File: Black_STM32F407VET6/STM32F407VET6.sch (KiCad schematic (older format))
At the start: 93 parts, among them J1 T0, J10 - HotBed +, J11 Heater0, J12 X-, J13 Y-, J14 Z-, J15 Z+, J16 USB_B, J2 T1, J22 Left, J23 EXP2, J24 LCD2004, J25 Bottom, J26 Right, J28 LIGHTS, J29 Z, J3 TB, J30 Z, J38 X, J39 Y, J4 TC, J41 E0, J43 Heater1, J44 COM, J47 I2C, J48 SPI, J49 SPI, J5 + VIN -, J50 SDIO, J51 Servo, J52 Servo, J53 PowerSelect, J54 Power, J55 PD11, J56 Power, J6 Fan3, J7 Fan2, J8 Fan1, J9 Fan0, Q1 BCX70, Q10 BCX70, Q11 BCX70, Q12 IRLR8726PBF, Q13 IRLR8726PBF, Q14 IRLR8726PBF, Q2 BCX70, Q3 BCX70, Q4 IRLML0030TRPBF, Q5 BCX70, Q6 IRLML0030TRPBF, Q7 IRLML0030TRPBF, Q8 IRLML0030TRPBF, Q9 BCX70, SW1 Boot0, U5 AT24CS01-SSHM

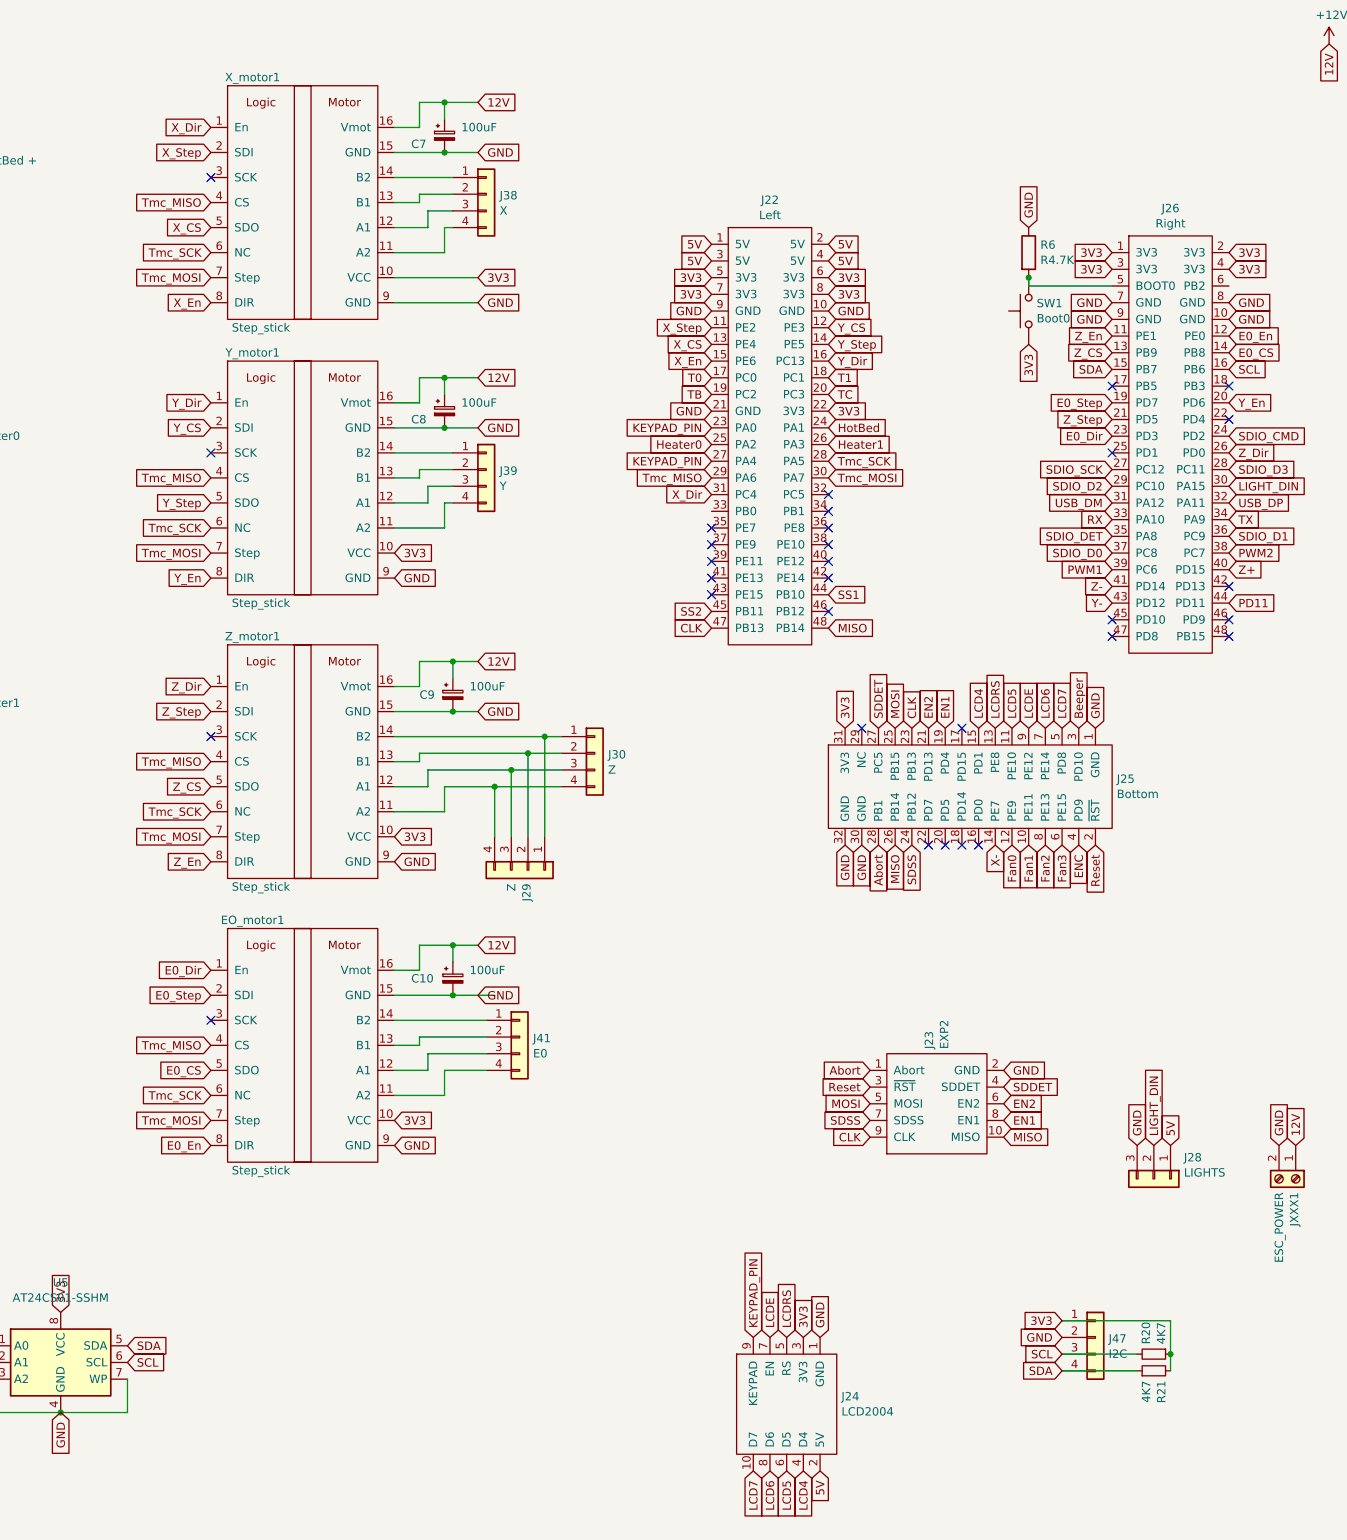
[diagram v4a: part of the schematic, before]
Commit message: Power connectors - Removed left side holes to make room for Heater and Bed traces - Moved spi connectors, temperature connectors, fan connectors - Assigned correct footprints to power connectors (KF7.62_2P) 	- Downloaded from: https://github.com/StefanHamminga/SH_Connectors.pretty
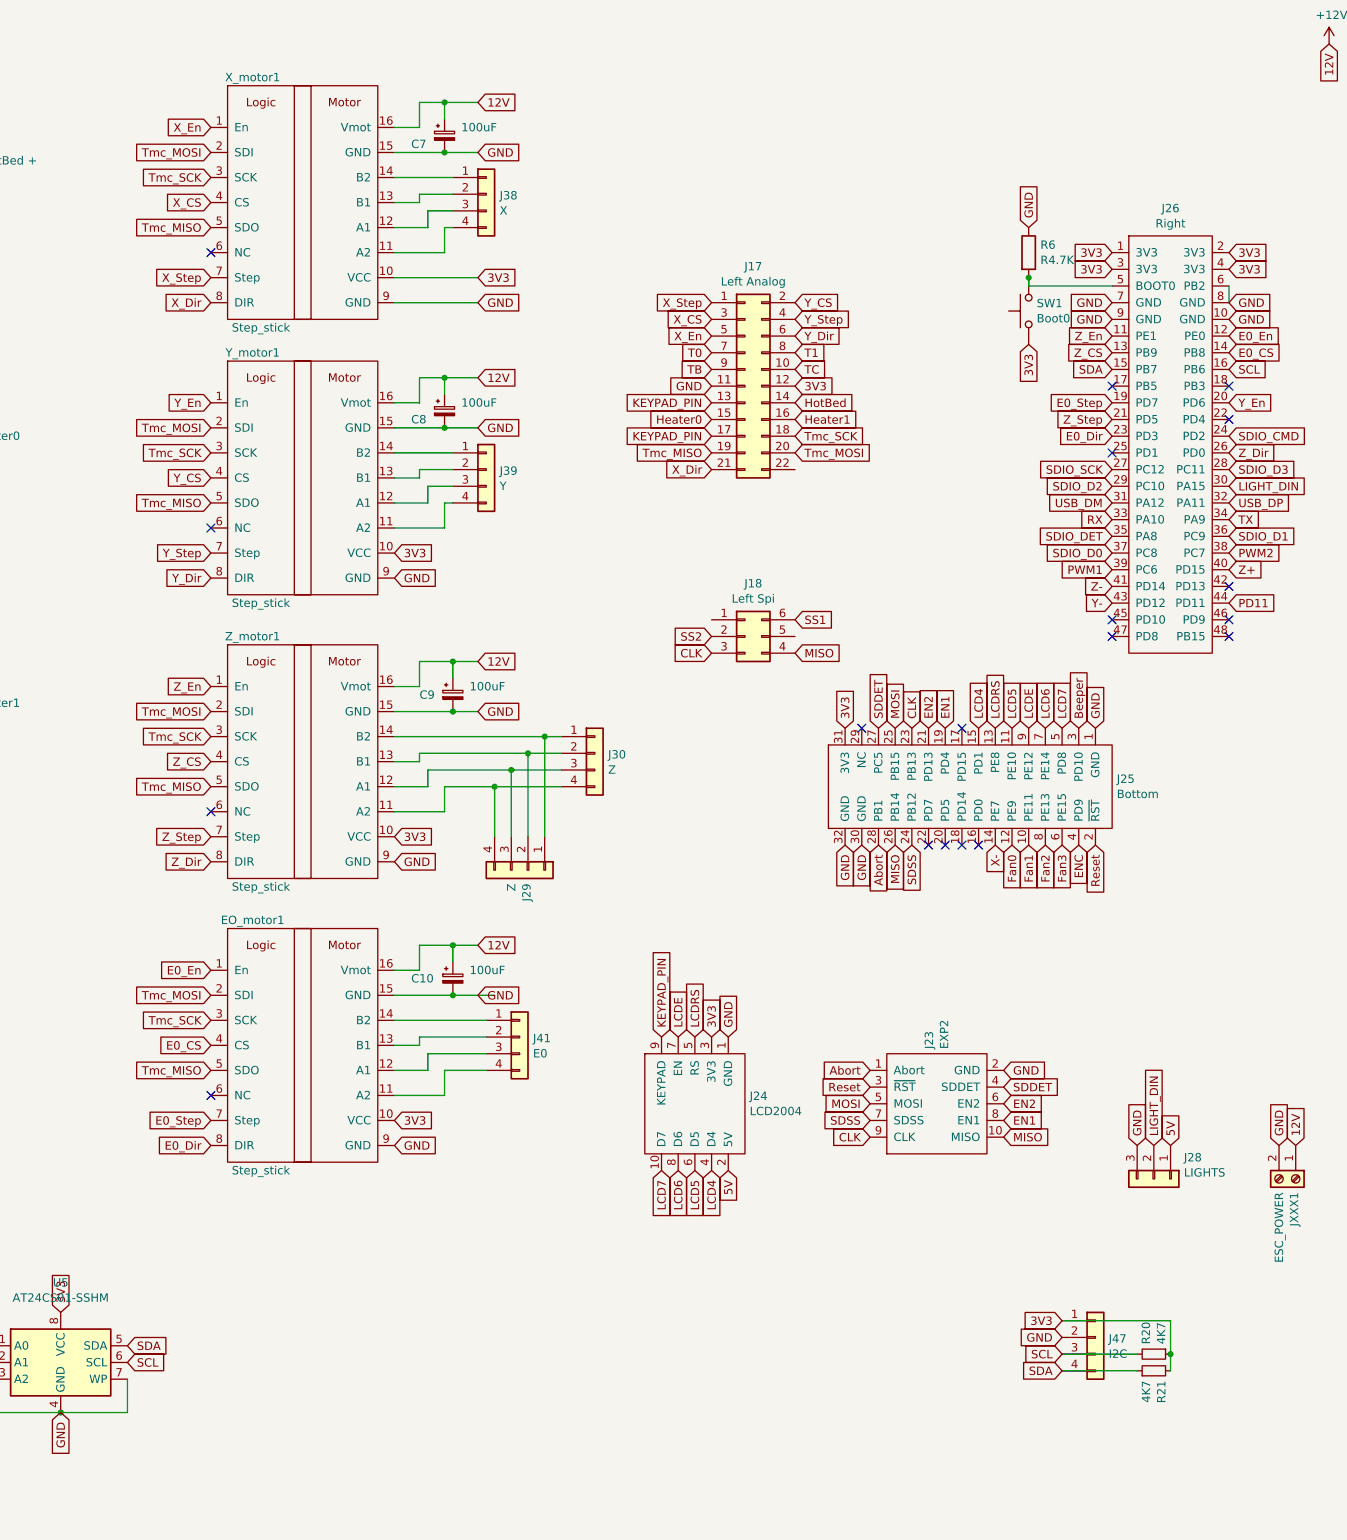
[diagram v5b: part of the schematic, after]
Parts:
- removed J22: Left, Connector_PinSocket_2.54mm:PinSocket_2x24_P2.54mm_Vertical, symbol STM32F407VET6:Left
- added J17: Left Analog, Connector_PinHeader_2.54mm:PinHeader_2x11_P2.54mm_Vertical, symbol Connector_Generic:Conn_02x11_Odd_Even
- added J18: Left Spi, Connector_PinHeader_2.54mm:PinHeader_2x03_P2.54mm_Vertical, symbol Connector_Generic:Conn_02x03_Counter_Clockwise
- J10: footprint Connector_JST:JST_XH_B2B-XH-A_1x02_P2.50mm_Vertical -> SH_Connectors:KF7.62_2P
- J11: footprint Connector_JST:JST_XH_B2B-XH-A_1x02_P2.50mm_Vertical -> TerminalBlock:TerminalBlock_bornier-2_P5.08mm
- J24: footprint Connector_JST:JST_XH_B10B-XH-A_1x10_P2.50mm_Vertical -> Connector_IDC:IDC-Header_2x05_P2.54mm_Vertical
- J43: footprint Connector_JST:JST_XH_B2B-XH-AM_1x02_P2.50mm_Vertical -> TerminalBlock:TerminalBlock_bornier-2_P5.08mm
- J5: footprint TerminalBlock_MetzConnect:TerminalBlock_MetzConnect_Type055_RT01502HDWU_1x02_P5.00mm_Horizontal -> SH_Connectors:KF7.62_2P
- JXXX1: footprint TerminalBlock_MetzConnect:TerminalBlock_MetzConnect_Type055_RT01502HDWU_1x02_P5.00mm_Horizontal -> TerminalBlock:TerminalBlock_bornier-2_P5.08mm
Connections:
- net +3V3: now also J17.12 (Pin_12)
- net CLK: now also J18.3 (Pin_3)
- net E0_CS: now also EO_motor1.4 (CS); no longer EO_motor1.5 (SDO)
- net E0_Dir: now also EO_motor1.8 (DIR); no longer EO_motor1.1 (En)
- net E0_En: now also EO_motor1.1 (En); no longer EO_motor1.8 (DIR)
- net E0_Step: now also EO_motor1.7 (Step); no longer EO_motor1.2 (SDI)
- net GND: now also J26.6 (PB2), J17.11 (Pin_11)
- net Heater0: now also J17.15 (Pin_15)
- net Heater1: now also J17.16 (Pin_16)
- net HotBed: now also J17.14 (Pin_14)
- net KEYPAD_PIN: now also J17.13 (Pin_13), J17.17 (Pin_17)
- net MISO: now also J18.4 (Pin_4)
- net SS1: now also J18.6 (Pin_6)
- net SS2: now also J18.2 (Pin_2)
- net T0: now also J17.7 (Pin_7)
- net T1: now also J17.8 (Pin_8)
- net TB: now also J17.9 (Pin_9)
- net TC: now also J17.10 (Pin_10)
- net Tmc_MISO: now also EO_motor1.5 (SDO), X_motor1.5 (SDO), Y_motor1.5 (SDO), Z_motor1.5 (SDO), J17.19 (Pin_19); no longer EO_motor1.4 (CS), X_motor1.4 (CS), Y_motor1.4 (CS), Z_motor1.4 (CS)
- net Tmc_MOSI: now also EO_motor1.2 (SDI), X_motor1.2 (SDI), Y_motor1.2 (SDI), Z_motor1.2 (SDI), J17.20 (Pin_20); no longer EO_motor1.7 (Step), X_motor1.7 (Step), Y_motor1.7 (Step), Z_motor1.7 (Step)
- net Tmc_SCK: now also EO_motor1.3 (SCK), X_motor1.3 (SCK), Y_motor1.3 (SCK), Z_motor1.3 (SCK), J17.18 (Pin_18); no longer EO_motor1.6 (NC), X_motor1.6 (NC), Y_motor1.6 (NC), Z_motor1.6 (NC)
- net X_CS: now also X_motor1.4 (CS), J17.3 (Pin_3); no longer X_motor1.5 (SDO)
- net X_Dir: now also X_motor1.8 (DIR), J17.21 (Pin_21); no longer X_motor1.1 (En)
- net X_En: now also X_motor1.1 (En), J17.5 (Pin_5); no longer X_motor1.8 (DIR)
- net X_Step: now also X_motor1.7 (Step), J17.1 (Pin_1); no longer X_motor1.2 (SDI)
- net Y_CS: now also Y_motor1.4 (CS), J17.2 (Pin_2); no longer Y_motor1.2 (SDI)
- net Y_Dir: now also Y_motor1.8 (DIR), J17.6 (Pin_6); no longer Y_motor1.1 (En)
- net Y_En: now also Y_motor1.1 (En); no longer Y_motor1.8 (DIR)
- net Y_Step: now also Y_motor1.7 (Step), J17.4 (Pin_4); no longer Y_motor1.5 (SDO)
- net Z_CS: now also Z_motor1.4 (CS); no longer Z_motor1.5 (SDO)
- net Z_Dir: now also Z_motor1.8 (DIR); no longer Z_motor1.1 (En)
- net Z_En: now also Z_motor1.1 (En); no longer Z_motor1.8 (DIR)
- net Z_Step: now also Z_motor1.7 (Step); no longer Z_motor1.2 (SDI)
- no-connect marks 31 -> 19
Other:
- moved on the sheet: J24
